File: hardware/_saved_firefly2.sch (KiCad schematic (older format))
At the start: 18 parts, among them J2 614105150721, J3 CONN_01X01, P3 CONN_01X04, P4 CONN_01X05, P5 CONN_01X01, U1 SAMD21E18, U2 RFM69CW, U3 MIC5504

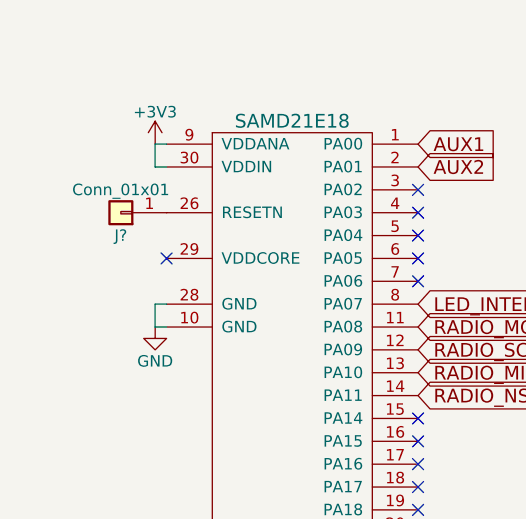
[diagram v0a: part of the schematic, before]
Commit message: Board rev 2.3
- Fix orientation for UC (in homebrew)
- Fix 3v3 -> 5v on programming header silk
- Flipped headers so the bottom has actual pads
- Exposed the reset pin
- Fixed LED signal shorted to ground pour

Change-Id: I21f070da93fd6e851c38ed11e53aa0c7e677237e
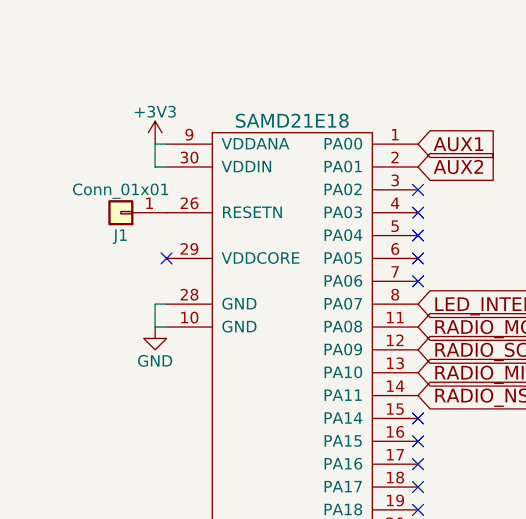
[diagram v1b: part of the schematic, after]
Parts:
- J1: renamed from J?; footprint (none) -> Pin_Headers:Pin_Header_Straight_1x01_Pitch1.27mm
- J3: footprint (none) -> Pin_Headers:Pin_Header_Straight_1x01_Pitch1.27mm
- P3: footprint Pin_Headers:Pin_Header_Straight_1x04_Pitch2.54mm -> Sparkfun-Connectors:1X04
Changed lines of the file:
@@
 F 0 "P3" H 3750 7650 50  0000 C CNN
 F 1 "CONN_01X04" V 3850 7400 50  0000 C CNN
-F 2 "Pin_Headers:Pin_Header_Straight_1x04_Pitch2.54mm" H 3750 7400 50  0001 C CNN
+F 2 "Sparkfun-Connectors:1X04" H 3750 7400 50  0001 C CNN
 F 3 "" H 3750 7400 50  0000 C CNN
 	1    3750 7400
@@
 F 0 "J3" H 8050 750 50  0000 C CNN
 F 1 "CONN_01X01" V 8150 650 50  0000 C CNN
-F 2 "" H 8050 650 50  0001 C CNN
+F 2 "Pin_Headers:Pin_Header_Straight_1x01_Pitch1.27mm" H 8050 650 50  0001 C CNN
 F 3 "" H 8050 650 50  0001 C CNN
 	1    8050 650
@@
 	8350 850  8050 850
 $Comp
-L Conn_01x01 J?
+L Conn_01x01 J1
 U 1 1 5B396353
 P 1000 1350
-F 0 "J?" H 1000 1450 50  0000 C CNN
+F 0 "J1" H 1000 1450 50  0000 C CNN
 F 1 "Conn_01x01" H 1000 1250 50  0000 C CNN
-F 2 "" H 1000 1350 50  0001 C CNN
+F 2 "Pin_Headers:Pin_Header_Straight_1x01_Pitch1.27mm" H 1000 1350 50  0001 C CNN
 F 3 "" H 1000 1350 50  0001 C CNN
 	1    1000 1350
